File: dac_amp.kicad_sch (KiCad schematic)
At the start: 21 parts, among them U16 NE5532

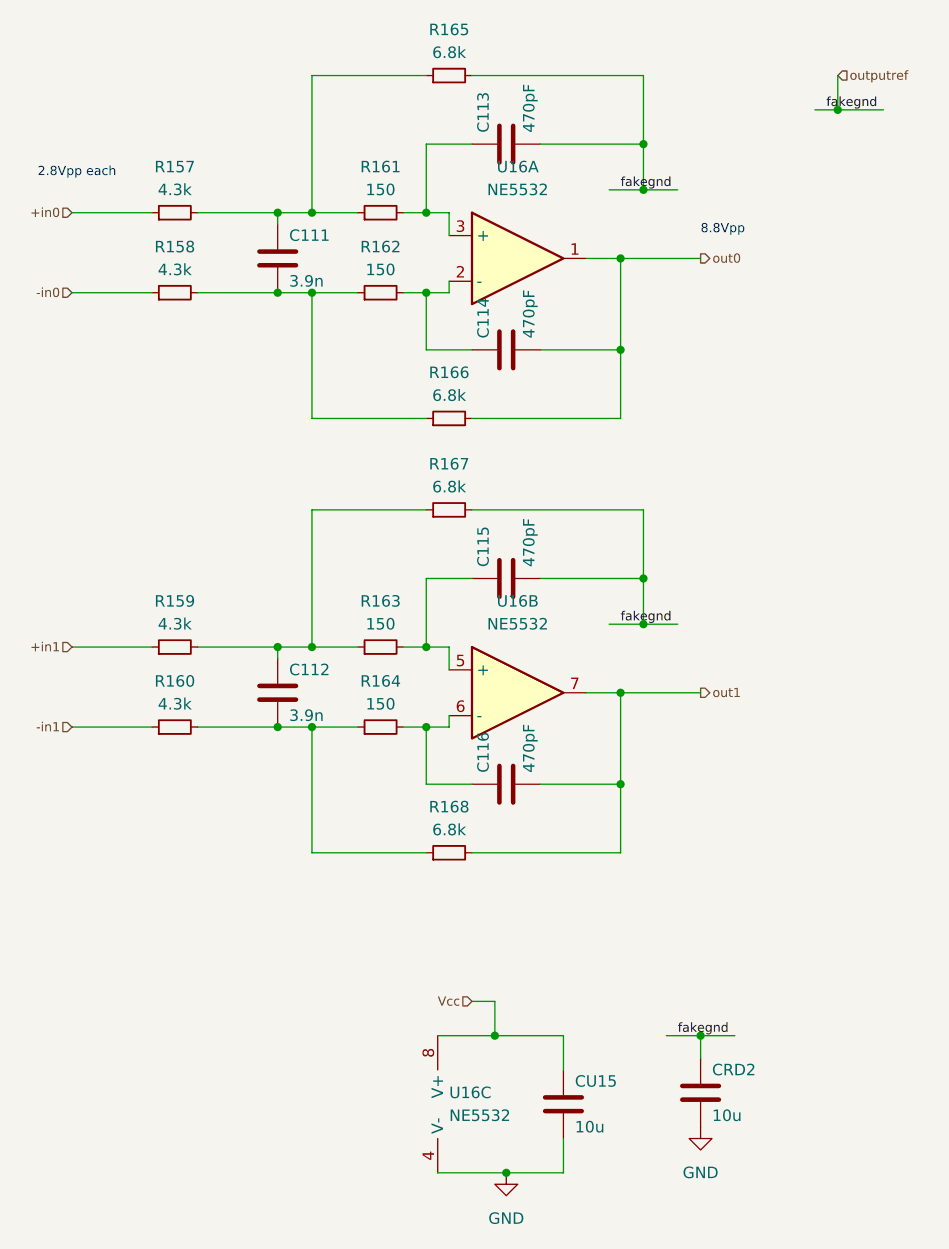
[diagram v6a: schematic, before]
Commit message: workaround major gain/signal margin error
using the components i have at hand. There probably are better options. Next revision should make use of the -5v rail.
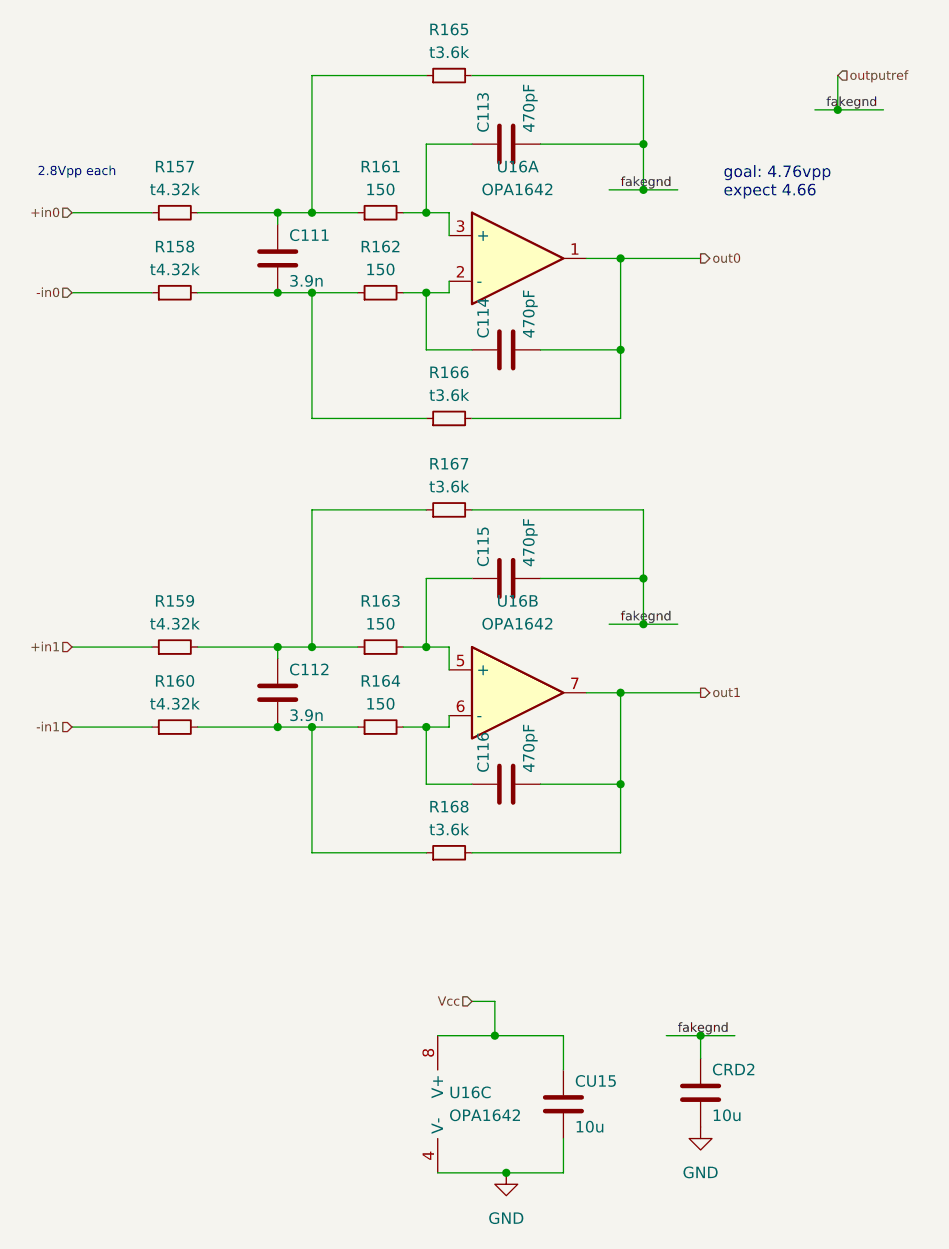
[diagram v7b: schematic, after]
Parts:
- R157, R158, R159, R160: value 4.3k -> t4.32k
- R165, R166, R167, R168: value 6.8k -> t3.6k
- U16: value NE5532 -> OPA1642
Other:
- note added: "goal: 4.76vpp expect 4.66"
- note removed: "8.8Vpp"
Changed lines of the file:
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@@
 		)
 	)
-	(text "2.8Vpp each"
+	(text "goal: 4.76vpp\nexpect 4.66"
 		(exclude_from_sim no)
-		(at 15.24 31.75 0)
+		(at 91.44 34.036 0)
 		(effects
 			(font
-				(size 1.016 1.016)
+				(size 1.27 1.27)
 			)
 			(justify left bottom)
 		)
 	)
-	(text "8.8Vpp"
+	(text "2.8Vpp each"
 		(exclude_from_sim no)
-		(at 88.9 38.1 0)
+		(at 15.24 31.75 0)
 		(effects
 			(font
@@
 			)
 		)
-		(property "Value" "4.3k"
+		(property "Value" "t4.32k"
 			(at 30.48 33.02 90)
 			(effects
@@
 			)
 		)
-		(property "Value" "6.8k"
+		(property "Value" "t3.6k"
 			(at 60.96 55.88 90)
 			(effects
@@
 			)
 		)
-		(property "Value" "NE5532"
+		(property "Value" "OPA1642"
 			(at 68.58 33.02 0)
 			(effects
@@
 			)
 		)
-		(property "Value" "6.8k"
+		(property "Value" "t3.6k"
 			(at 60.96 104.14 90)
 			(effects
@@
 			)
 		)
-		(property "Value" "4.3k"
+		(property "Value" "t4.32k"
 			(at 30.48 81.28 90)
 			(effects
@@
 			)
 		)
-		(property "Value" "4.3k"
+		(property "Value" "t4.32k"
 			(at 30.48 41.91 90)
 			(effects
@@
 			)
 		)
-		(property "Value" "4.3k"
+		(property "Value" "t4.32k"
 			(at 30.48 90.17 90)
 			(effects
@@
 			)
 		)
-		(property "Value" "6.8k"
+		(property "Value" "t3.6k"
 			(at 60.96 17.78 90)
 			(effects
@@
 			)
 		)
-		(property "Value" "NE5532"
+		(property "Value" "OPA1642"
 			(at 60.96 135.8899 0)
 			(effects
@@
 			)
 		)
-		(property "Value" "6.8k"
+		(property "Value" "t3.6k"
 			(at 60.96 66.04 90)
 			(effects
@@
 			)
 		)
-		(property "Value" "NE5532"
+		(property "Value" "OPA1642"
 			(at 68.58 81.28 0)
 			(effects

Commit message: work on bugs...
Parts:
- U16: value OPA1642 -> MC33078; PN NE5532DR -> MC33078
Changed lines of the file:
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@@
 			)
 		)
-		(property "Value" "OPA1642"
+		(property "Value" "MC33078"
 			(at 68.58 33.02 0)
 			(effects
@@
 			)
 		)
-		(property "PN" "NE5532DR"
+		(property "PN" "MC33078"
 			(at 68.58 40.64 0)
 			(effects
@@
 			)
 		)
-		(property "Value" "OPA1642"
+		(property "Value" "MC33078"
 			(at 60.96 135.8899 0)
 			(effects
@@
 			)
 		)
-		(property "PN" "NE5532DR"
+		(property "PN" "MC33078"
 			(at 62.23 134.62 0)
 			(effects
@@
 			)
 		)
-		(property "Value" "OPA1642"
+		(property "Value" "MC33078"
 			(at 68.58 81.28 0)
 			(effects
@@
 			)
 		)
-		(property "PN" "NE5532DR"
+		(property "PN" "MC33078"
 			(at 68.58 88.9 0)
 			(effects
